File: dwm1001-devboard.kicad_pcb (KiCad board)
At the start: 2 copper layers, 52.6 x 48.8 mm, 45 parts, among them J1 Micro USB B, J2 SWD Pin Header Male, J4 15, J5 Tag-Connect TC2030 SWD, J6 8, J7 10, Q1 FDN430P, Q2 FDN430P, SW1 RST, SW2 WKUP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

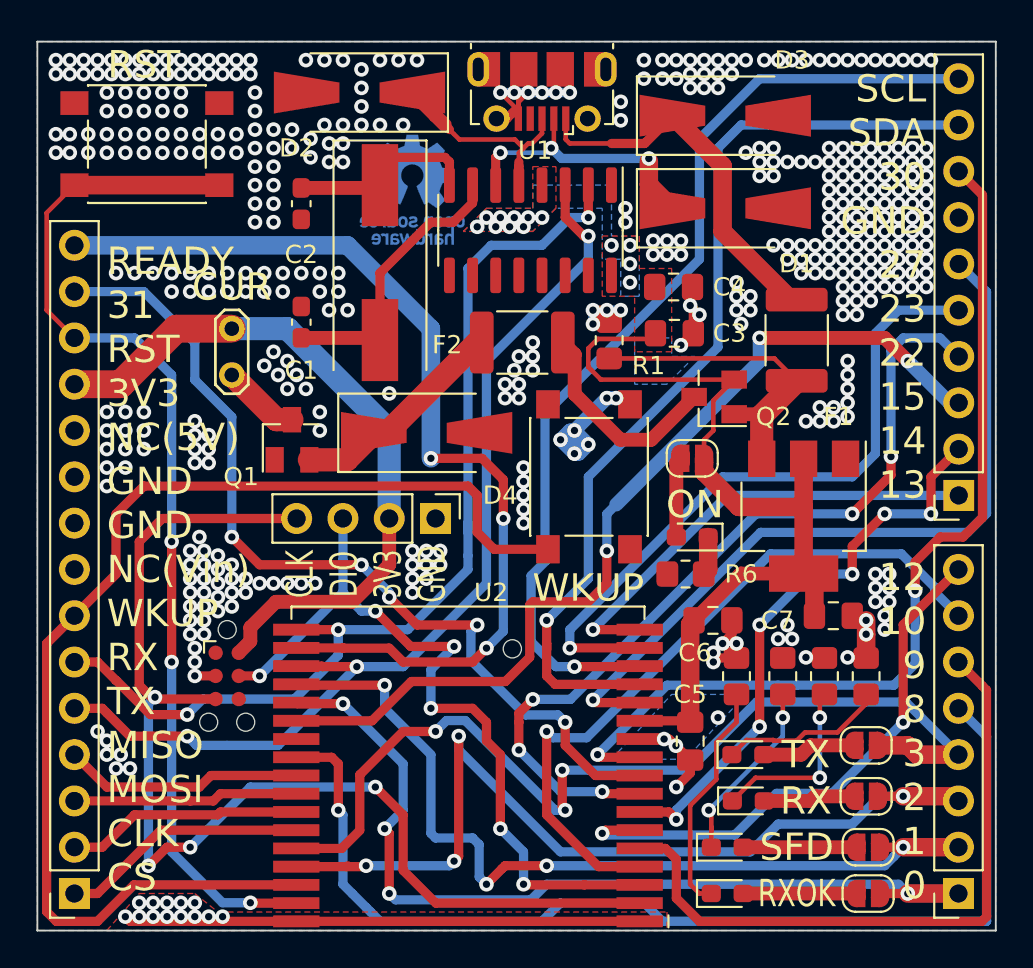
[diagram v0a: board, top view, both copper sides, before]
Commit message: get rid of solder jumpers
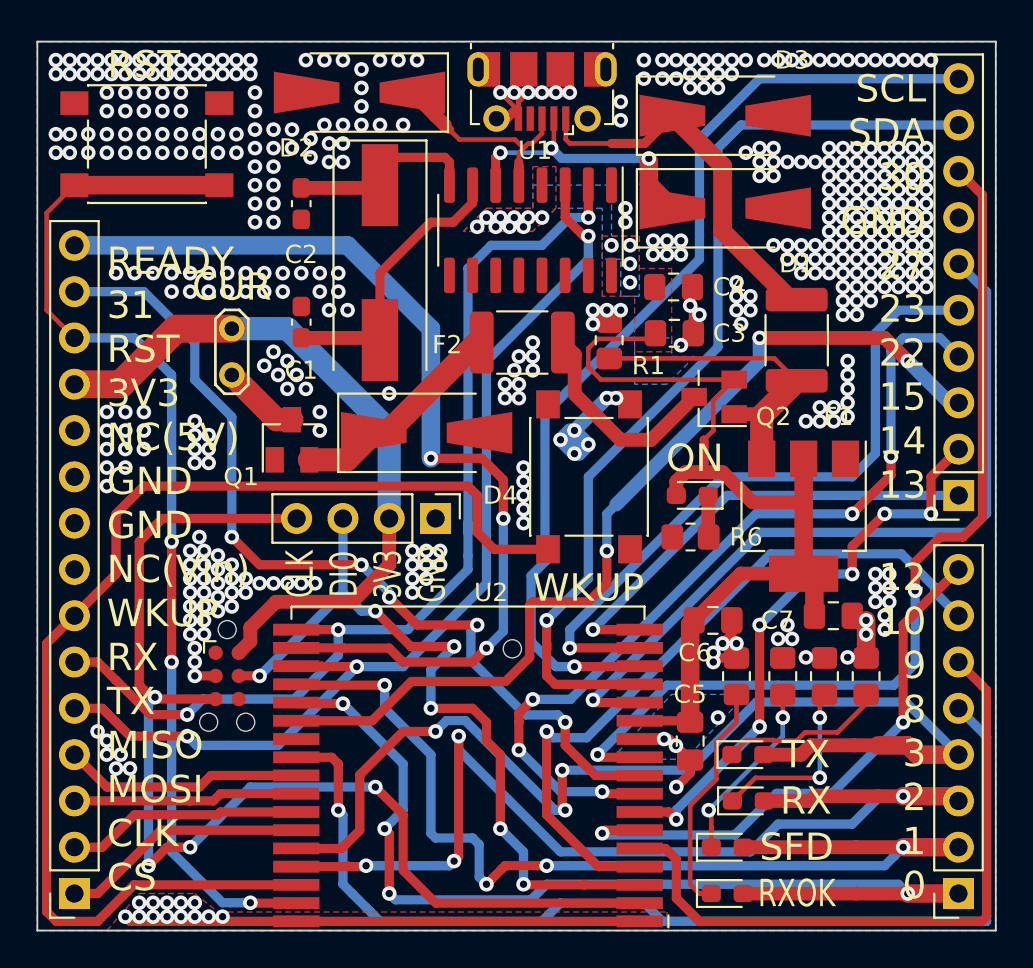
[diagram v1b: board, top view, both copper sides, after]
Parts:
- removed JP2: RXOKLED, Jumper:SolderJumper-2_P1.3mm_Open_RoundedPad1.0x1.5mm
- removed JP3: SFDLED, Jumper:SolderJumper-2_P1.3mm_Open_RoundedPad1.0x1.5mm
- removed JP4: RXLED, Jumper:SolderJumper-2_P1.3mm_Open_RoundedPad1.0x1.5mm
- removed JP5: TXLED, Jumper:SolderJumper-2_P1.3mm_Open_RoundedPad1.0x1.5mm
- removed JP6: PWRLED, Jumper:SolderJumper-2_P1.3mm_Open_RoundedPad1.0x1.5mm
- removed REF**: OSHW-Logo_5.7x6mm_Copper, Symbol:OSHW-Logo_5.7x6mm_Copper
- moved D9 2.29 mm to (144.4, 88.4)
- moved R6 2.05 mm to (144.3, 90.7)
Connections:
- D5 pad 2: Net-(D5-Pad2) -> /GPIO0
- D6 pad 2: Net-(D6-Pad2) -> /GPIO1
- D7 pad 2: Net-(D7-Pad2) -> /GPIO2
- D8 pad 2: Net-(D8-Pad2) -> /GPIO3
- D9 pad 2: Net-(D9-Pad2) -> +3V3
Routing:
- net /GPIO1: track 47.3 -> 54.9 mm
- net /GPIO0: track 48.4 -> 55.9 mm
- net /GPIO3: track 52.9 -> 59.4 mm
- net /GPIO2: track 49.1 -> 55.4 mm
- net Net-(D6-Pad2): track 6.32 -> 0.00 mm
- net Net-(D5-Pad2): track 6.21 -> 0.00 mm
- net Net-(D8-Pad2): track 5.20 -> 0.00 mm
- net Net-(D7-Pad2): track 5.04 -> 0.00 mm
- net Net-(D9-Pad2): track 4.41 -> 0.00 mm
- net +3V3: track 50.3 -> 52.8 mm
